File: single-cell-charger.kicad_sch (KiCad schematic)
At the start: 20 parts, among them Q1 DMG6968UDM-7, U2 BQ2970

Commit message: finished schematic; (major parts selected)
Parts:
- added R62: 100, symbol Device:R_Small
- D1: value BLUE_LED -> BLUE_LED3.5V
- D2: value RED_LED -> RED_LED2V
- R2: value 330 -> 200
- R3: value 330 -> 100
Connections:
- net BAT-: now also R62.2; no longer Q1.1 (D1)
- new net: Q1.1 (D1), R62.1
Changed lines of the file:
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@@
     (stroke (width 0) (type default))
   )
-  (wire (pts (xy 196.85 106.68) (xy 242.57 106.68))
+  (wire (pts (xy 196.85 106.68) (xy 217.17 106.68))
     (stroke (width 0) (type default))
   )
@@
     (stroke (width 0) (type default))
   )
+  (wire (pts (xy 222.25 106.68) (xy 242.57 106.68))
+    (stroke (width 0) (type default))
+  )
   (wire (pts (xy 111.76 96.52) (xy 111.76 99.06))
     (stroke (width 0) (type default))
@@
     (stroke (width 0) (type default))
   )
-  (text_box "increase to reduce charge current from 800ma"
-    (at 82.55 104.14 0) (size 27.94 5.08)
+  (text_box "increase from 0 to reduce charge current from 800ma"
+    (at 97.79 104.14 0) (size 12.7 5.08)
     (stroke (width 0) (type default))
     (fill (type none))
-    (effects (font (size 1.1 1.1)) (justify left top))
+    (effects (font (size 0.7 0.7)) (justify left top))
+  )
+  (text_box "Replace with 0ohm if needed"
+    (at 213.36 110.49 0) (size 11.43 2.54)
+    (stroke (width 0) (type default))
+    (fill (type none))
+    (effects (font (size 0.5 0.5)) (justify left top))
+  )
+  (text_box "±1% tolerance resistor with <200 ppm/ºC"
+    (at 163.83 93.98 0) (size 7.62 3.81)
+    (stroke (width 0) (type default))
+    (fill (type none))
+    (effects (font (size 0.5 0.5)) (justify left top))
   )
   (text "DNP" (at 116.84 77.47 0)
@@
     )
   )
+  (symbol (lib_id "Device:R_Small") (at 219.71 106.68 90) (unit 1)
+    (in_bom yes) (on_board yes) (dnp no)
+    (property "Reference" "R62" (at 219.71 109.22 90)
+      (effects (font (size 1.27 1.27)))
+    )
+    (property "Value" "100" (at 219.71 104.14 90)
+      (effects (font (size 1.27 1.27)))
+    )
+    (property "Footprint" "" (at 219.71 106.68 0)
+      (effects (font (size 1.27 1.27)) hide)
+    )
+    (property "Datasheet" "~" (at 219.71 106.68 0)
+      (effects (font (size 1.27 1.27)) hide)
+    )
+    (pin "1")
+    (pin "2")
+    (instances
+      (project "rocket2-battery"
+        (path "/453543af-7e3c-49a0-a644-4bd49c4f86f8/a9e32f45-e2eb-48cf-a7f9-7bedc8d925bf"
+          (reference "R62") (unit 1)
+        )
+        (path "/453543af-7e3c-49a0-a644-4bd49c4f86f8/353f4db0-8115-4c24-a632-6a043c6847b5"
+          (reference "R63") (unit 1)
+        )
+        (path "/453543af-7e3c-49a0-a644-4bd49c4f86f8/f3a6411d-fb1d-4837-a6de-b74ae1f1a96c"
+          (reference "R64") (unit 1)
+        )
+        (path "/453543af-7e3c-49a0-a644-4bd49c4f86f8/b17bc1f0-00f5-4207-bf92-ef7f43c361e6"
+          (reference "R65") (unit 1)
+        )
+        (path "/453543af-7e3c-49a0-a644-4bd49c4f86f8/9511d0eb-6ca7-4945-a6c9-56e27962d3ed"
+          (reference "R66") (unit 1)
+        )
+        (path "/453543af-7e3c-49a0-a644-4bd49c4f86f8/771af3e6-8a40-4ded-b6c1-1f6c75fa6bde"
+          (reference "R67") (unit 1)
+        )
+      )
+    )
+  )
   (symbol (lib_id "Device:R_Small") (at 172.72 99.06 0) (unit 1)
     (in_bom yes) (on_board yes) (dnp no)
@@
       (effects (font (size 1.27 1.27)))
     )
-    (property "Value" "330" (at 147.32 105.41 90)
+    (property "Value" "100" (at 147.32 105.41 90)
       (effects (font (size 1.27 1.27)))
     )
@@
       (effects (font (size 1.27 1.27)))
     )
-    (property "Value" "330" (at 160.02 105.41 90)
+    (property "Value" "200" (at 160.02 105.41 90)
       (effects (font (size 1.27 1.27)))
     )
@@
       (effects (font (size 1.27 1.27)) (justify left))
     )
-    (property "Value" "BLUE_LED" (at 140.97 99.695 90)
+    (property "Value" "BLUE_LED3.5V" (at 137.16 99.695 90)
       (effects (font (size 1.27 1.27)) (justify left))
     )
@@
       (effects (font (size 1.27 1.27)) hide)
     )
-    (property "Datasheet" "https://www.qt-brightek.com/datasheet/QBLP670D_series.pdf" (at 151.13 97.79 90)
+    (property "Datasheet" "" (at 151.13 97.79 90)
       (effects (font (size 1.27 1.27)) hide)
     )
@@
       (effects (font (size 1.27 1.27)) (justify left))
     )
-    (property "Value" "RED_LED" (at 156.845 99.695 90)
+    (property "Value" "RED_LED2V" (at 156.845 99.695 90)
       (effects (font (size 1.27 1.27)) (justify left))
     )
@@
       (effects (font (size 1.27 1.27)) hide)
     )
-    (property "Datasheet" "https://www.qt-brightek.com/datasheet/QBLP670D_series.pdf" (at 154.94 97.79 90)
-      (effects (font (size 1.27 1.27)) hide)
-    )
+    (property "Datasheet" "" (at 154.94 97.79 90)
+      (effects (font (size 1.27 1.27)) hide)
+    )

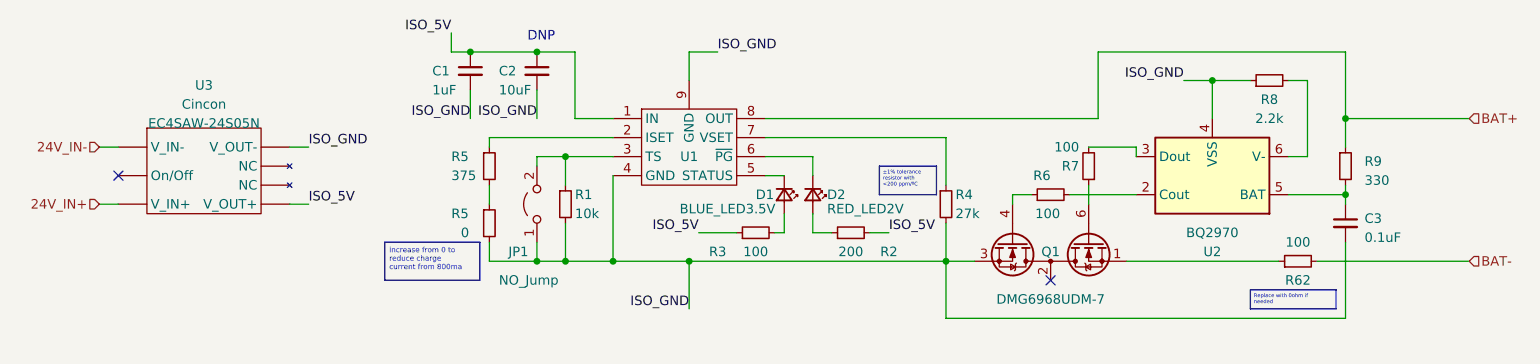
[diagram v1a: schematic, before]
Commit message: Updated schematic with symbols and footprints
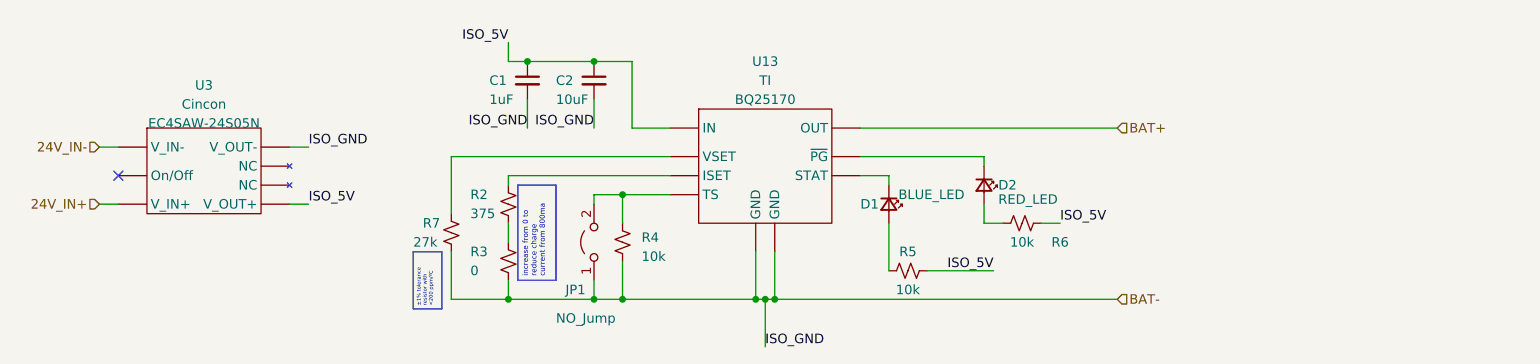
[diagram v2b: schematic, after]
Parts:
- removed C3: 0.1uF, symbol Device:C_Small
- removed Q1: DMG6968UDM-7, Package_TO_SOT_SMD:SOT-23-6, symbol Transistor_FET:DMG9926UDM
- removed R1: 10k, symbol Device:R_Small
- removed R2: 200, symbol Device:R_Small
- removed R3, R6, R62, R7: 100, symbol Device:R_Small
- removed R4: 27k, symbol Device:R_Small
- removed R5: 375, symbol Device:R_Small
- removed R5: 0, symbol Device:R_Small
- removed R8: 2.2k, symbol Device:R_Small
- removed R9: 330, symbol Device:R_Small
- removed U1: ~, Package_SON:WSON-8-1EP_2x2mm_P0.5mm_EP0.9x1.6mm_ThermalVias, symbol UCIRP-KiCAD-Lib:BQ25170
- removed U2: BQ2970, Package_SON:WSON-6_1.5x1.5mm_P0.5mm, symbol Battery_Management:BQ297xy
- added R2: 375, Resistor_SMD:R_0603_1608Metric_Pad0.98x0.95mm_HandSolder, symbol Device:R_Small_US
- added R3: 0, Resistor_SMD:R_1206_3216Metric_Pad1.30x1.75mm_HandSolder, symbol Device:R_Small_US
- added R4, R5, R6: 10k, Resistor_SMD:R_0603_1608Metric_Pad0.98x0.95mm_HandSolder, symbol Device:R_Small_US
- added R7: 27k, Resistor_SMD:R_0603_1608Metric_Pad0.98x0.95mm_HandSolder, symbol Device:R_Small_US
- added U13: ~, Package_SON:WSON-8-1EP_2x2mm_P0.5mm_EP0.9x1.6mm, symbol UCIRP-KiCAD-Lib:BQ25170
- C1, C2: footprint (none) -> Capacitor_SMD:C_0603_1608Metric_Pad1.08x0.95mm_HandSolder
- D1: value BLUE_LED3.5V -> BLUE_LED; footprint (none) -> LED_SMD:LED_0603_1608Metric_Pad1.05x0.95mm_HandSolder
- D2: value RED_LED2V -> RED_LED; footprint (none) -> LED_SMD:LED_0603_1608Metric_Pad1.05x0.95mm_HandSolder
- JP1: footprint (none) -> Connector_PinHeader_2.54mm:PinHeader_1x02_P2.54mm_Vertical
- U3: footprint (none) -> UCIRP-KiCAD-Lib:EC4SAW-xxSxxN
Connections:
- net ISO_GND is gone; now on net BAT-: C1.2, C2.2, JP1.1 (A), U3.7 (V_OUT-)
- net BAT+: now also U13.8 (OUT)
- net BAT-: now also R3.1, R4.2, R7.2, U13.4 (GND), U13.9 (GND)
- net ISO_5V: now also R5.2, R6.2, U13.1 (IN)
- net at JP1.2 (B): now also R4.1, U13.3 (TS)
- net at D1.2 (A): now also R5.1
- net at D2.2 (A): now also R6.1
- net at D1.1 (K): now also U13.5 (STAT)
- net at D2.1 (K): now also U13.6 (~{PG})
- new net: R2.1, R3.2
- new net: R7.1, U13.7 (VSET)
- new net: R2.2, U13.2 (ISET)
- no-connect marks 2 -> 1
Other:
- note removed: "DNP"
- moved on the sheet: C1, C2, D1, D2

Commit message: Finished Schematic; Time to Review
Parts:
- removed U3: ~, UCIRP-KiCAD-Lib:EC4SAW-xxSxxN, symbol UCIRP-KiCAD-Lib:EC4SAW
- added U4: ~, Package_SIP:SIP-8_19x3mm_P2.54mm, symbol UCIRP-KiCAD-Lib:EC4SAW-xxSxxN
- C1, C2, D1, D2, JP1: Manufacturer (none) -> Generic
- R17: renamed from R2; Manufacturer (none) -> Generic
- R18: renamed from R3; Manufacturer (none) -> Generic
- R19: renamed from R4; Manufacturer (none) -> Generic
- R20: renamed from R5; Manufacturer (none) -> Generic
- R21: renamed from R6; Manufacturer (none) -> Generic
- renumbered R7 to R16, U13 to U5
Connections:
- net 24V_IN+: now also U4.2 (VIN+)
- net 24V_IN-: now also U4.1 (VIN-)
- net BAT-: now also U4.7 (VOUT-)
- net ISO_5V: now also U4.6 (VOUT+)
- new net: U4.5, U4.8

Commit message: Fixed issues
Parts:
- C1: Part # (none) -> Generic 0603 1uF 6.3V X7R MLCC
- C2: Part # (none) -> Generic 0603 10uF 6.3V X7R MLCC
- D1: Part # (none) -> Generic 0603 Red LED
- D2: Part # (none) -> Generic 0603 Blue LED
- JP1: Part # (none) -> Generic 2.54mm 1x2 Pin Header
- R16: value 27k -> 27K
- R17: Part # (none) -> Generic 0603 375ohm 0.1% Resistor
- R18: Part # (none) -> Generic 0603 0ohm Resistor
- R19, R20, R21: value 10k -> 10K; Part # (none) -> Generic 0603 10K 1% Resistor
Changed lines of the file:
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@@
+      (effects (font (size 1.27 1.27)) hide)
+    )
+    (property "Part #" "Generic 0603 0ohm Resistor" (at 114.3 106.68 0)
       (effects (font (size 1.27 1.27)) hide)
     )
@@
     )
     (property "Manufacturer" "Generic" (at 125.73 104.14 0)
+      (effects (font (size 1.27 1.27)) hide)
+    )
+    (property "Part #" "Generic 2.54mm 1x2 Pin Header" (at 125.73 104.14 0)
       (effects (font (size 1.27 1.27)) hide)
     )
@@
       (effects (font (size 1.27 1.27)))
     )
-    (property "Value" "10k" (at 182.88 104.14 90)
+    (property "Value" "10K" (at 182.88 104.14 90)
       (effects (font (size 1.27 1.27)))
     )
@@
       (effects (font (size 1.27 1.27)) hide)
     )
+    (property "Part #" "Generic 0603 10K 1% Resistor" (at 182.88 101.6 0)
+      (effects (font (size 1.27 1.27)) hide)
+    )
     (pin "1")
     (pin "2")
@@
     )
     (property "Manufacturer" "Generic" (at 116.84 82.55 0)
+      (effects (font (size 1.27 1.27)) hide)
+    )
+    (property "Part #" "Generic 0603 1uF 6.3V X7R MLCC" (at 116.84 82.55 0)
       (effects (font (size 1.27 1.27)) hide)
     )
@@
       (effects (font (size 1.27 1.27)))
     )
-    (property "Value" "10k" (at 167.64 110.49 90)
+    (property "Value" "10K" (at 167.64 110.49 90)
       (effects (font (size 1.27 1.27)))
     )
@@
       (effects (font (size 1.27 1.27)) hide)
     )
+    (property "Part #" "Generic 0603 10K 1% Resistor" (at 167.64 107.95 0)
+      (effects (font (size 1.27 1.27)) hide)
+    )
     (pin "1")
     (pin "2")
@@
       (effects (font (size 1.27 1.27)) (justify left))
     )
-    (property "Value" "27k" (at 101.6 104.14 0)
+    (property "Value" "27K" (at 101.6 104.14 0)
       (effects (font (size 1.27 1.27)) (justify left))
     )
@@
       (effects (font (size 1.27 1.27)) (justify left))
     )
-    (property "Value" "10k" (at 132.08 106.045 0)
+    (property "Value" "10K" (at 132.08 106.045 0)
       (effects (font (size 1.27 1.27)) (justify left))
     )
@@
     )
     (property "Manufacturer" "Generic" (at 129.54 104.14 0)
+      (effects (font (size 1.27 1.27)) hide)
+    )
+    (property "Part #" "Generic 0603 10K 1% Resistor" (at 129.54 104.14 0)
       (effects (font (size 1.27 1.27)) hide)
     )
@@
     )
     (property "Manufacturer" "Generic" (at 114.3 99.06 0)
+      (effects (font (size 1.27 1.27)) hide)
+    )
+    (property "Part #" "Generic 0603 375ohm 0.1% Resistor" (at 114.3 99.06 0)
       (effects (font (size 1.27 1.27)) hide)
     )
@@
       (effects (font (size 1.27 1.27)) hide)
     )
+    (property "Part #" "Generic 0603 10uF 6.3V X7R MLCC" (at 125.73 82.55 0)
+      (effects (font (size 1.27 1.27)) hide)
+    )
     (pin "1")
     (pin "2")
@@
       (effects (font (size 1.27 1.27)) hide)
     )
+    (property "Part #" "Generic 0603 Red LED" (at 165.1 99.06 0)
+      (effects (font (size 1.27 1.27)) hide)
+    )
     (pin "1")
     (pin "2")
@@
       (effects (font (size 1.27 1.27)) hide)
     )
+    (property "Part #" "Generic 0603 Blue LED" (at 177.8 96.52 0)
+      (effects (font (size 1.27 1.27)) hide)
+    )

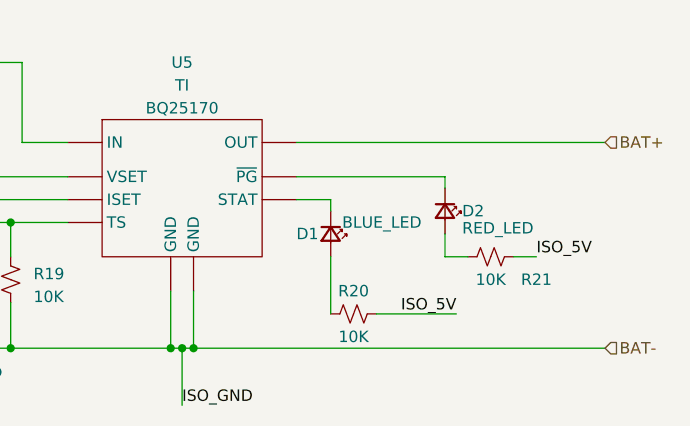
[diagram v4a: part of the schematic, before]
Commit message: Made Charging layout
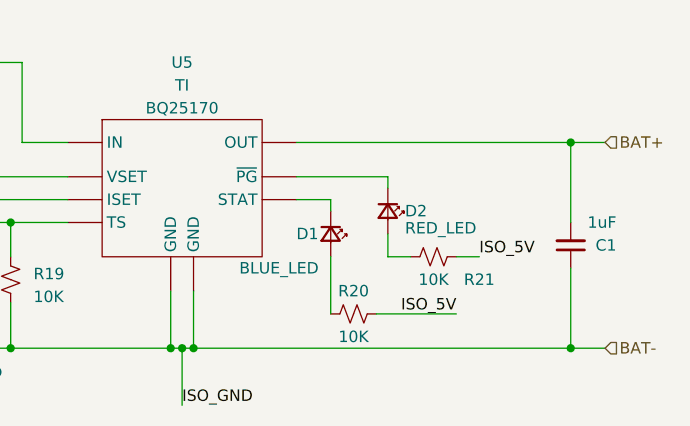
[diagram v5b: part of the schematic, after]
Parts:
- added C1: 1uF, Capacitor_SMD:C_0603_1608Metric_Pad1.08x0.95mm_HandSolder, symbol Device:C_Small
- U4: footprint Package_SIP:SIP-8_19x3mm_P2.54mm -> UCIRP-KiCAD-Lib:EC4SAW-xxSxxN
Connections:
- net BAT+: now also C1.2
- net BAT-: now also C1.1
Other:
- moved on the sheet: D2, R21

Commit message: some minor fixes
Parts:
- D1: Part # Generic 0603 Red LED -> Generic 0603 Blue LED
- D2: Part # Generic 0603 Blue LED -> Generic 0603 Red LED
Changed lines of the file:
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@@
       (effects (font (size 1.27 1.27)) hide)
     )
-    (property "Part #" "Generic 0603 Red LED" (at 165.1 99.06 0)
+    (property "Part #" "Generic 0603 Blue LED" (at 165.1 99.06 0)
       (effects (font (size 1.27 1.27)) hide)
     )
@@
       (effects (font (size 1.27 1.27)) hide)
     )
-    (property "Part #" "Generic 0603 Blue LED" (at 171.45 96.52 0)
+    (property "Part #" "Generic 0603 Red LED" (at 171.45 96.52 0)
       (effects (font (size 1.27 1.27)) hide)
     )
